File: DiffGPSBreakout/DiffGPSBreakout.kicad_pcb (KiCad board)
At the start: 2 copper layers, 110.2 x 72.3 mm, 16 parts, among them U1 Raspberry_Pi

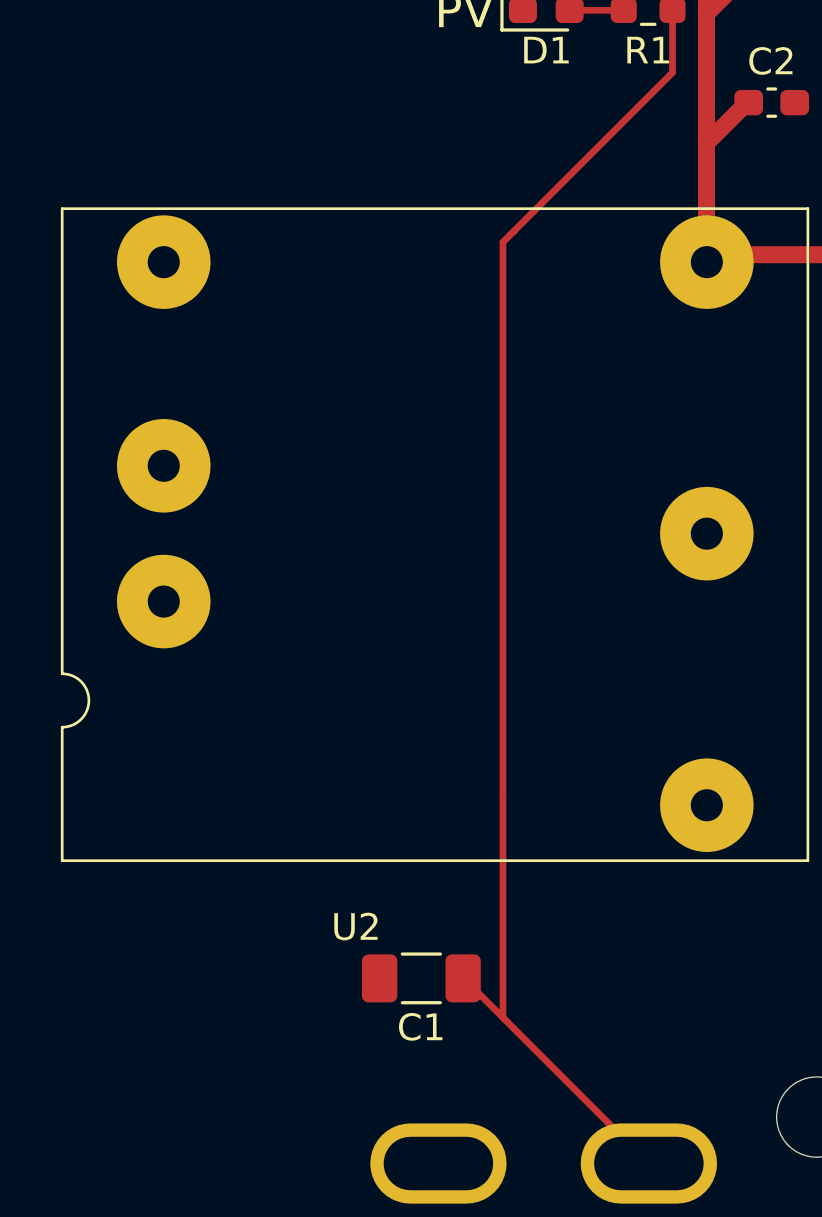
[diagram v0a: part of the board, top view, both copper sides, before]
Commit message: fixed traces
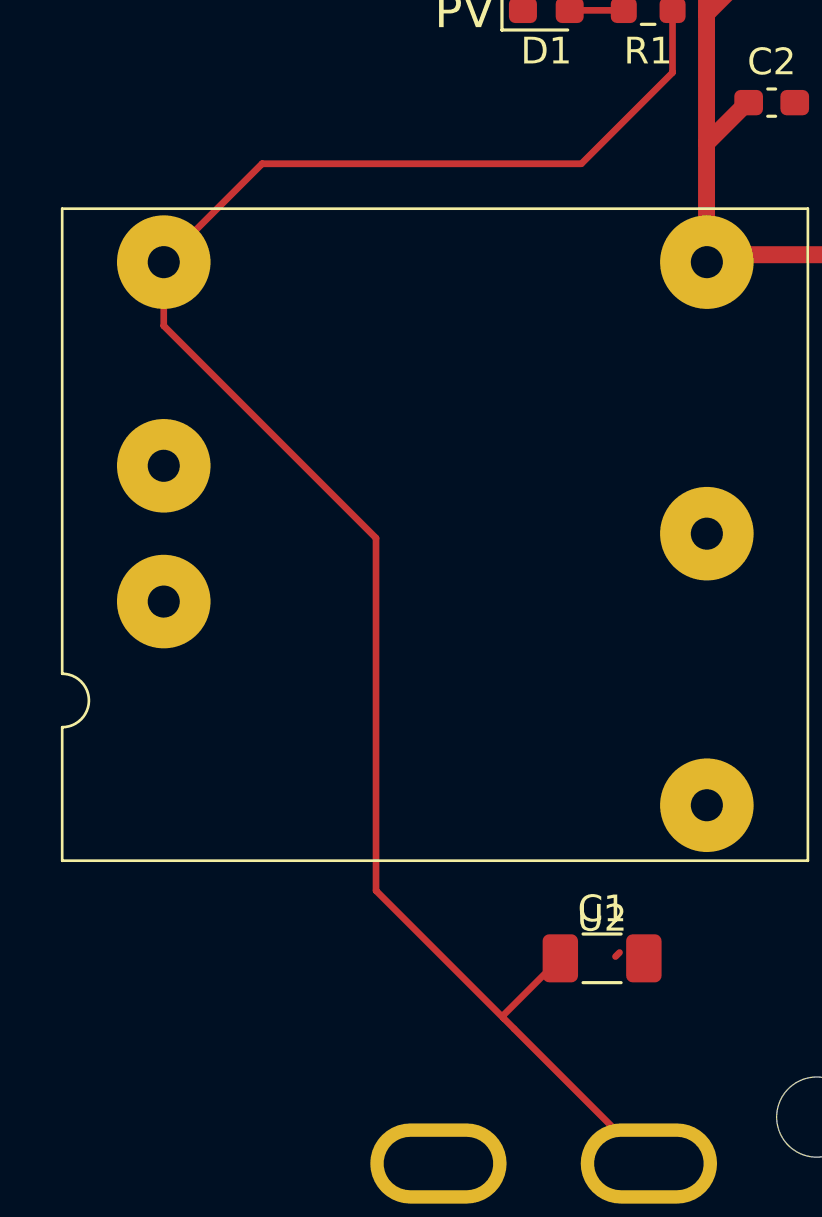
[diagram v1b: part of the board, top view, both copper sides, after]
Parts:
- moved C1 6.80 mm to (106.9, 107.4), turned to 0 degrees
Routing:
- net VCC: track 50.6 -> 69.3 mm
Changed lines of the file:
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@@
 		(at 86.734 103.7432)
 		(property "Reference" "U2"
-			(at 10.999999 2.494519 0)
+			(at 20.2 2.1494 0)
 			(unlocked yes)
 			(layer "F.SilkS")
@@
 		)
 		(property "Value" "~"
-			(at 10.999999 3.994519 0)
+			(at 20.2 3.6494 0)
 			(unlocked yes)
 			(layer "F.Fab")
@@
 		)
 		(fp_text user "${REFERENCE}"
-			(at 10.999999 5.494519 0)
+			(at 20.2 5.1494 0)
 			(unlocked yes)
 			(layer "F.Fab")
@@
 	(footprint "Capacitor_SMD:C_1206_3216Metric_Pad1.33x1.80mm_HandSolder"
 		(layer "F.Cu")
-		(at 100.172119 108.141401 180)
+		(at 106.934 107.3912)
 		(descr "Capacitor SMD 1206 (3216 Metric), square (rectangular) end terminal, IPC_7351 nominal with elongated pad for handsoldering. (Body size source: IPC-SM-782 page 76, https://www.pcb-3d.com/wordpress/wp-content/uploads/ipc-sm-782a_amendment_1_and_2.pdf), generated with kicad-footprint-generator")
 		(tags "capacitor handsolder")
 		(property "Reference" "C1"
-			(at 0 -1.85 180)
+			(at 0 -1.85 360)
 			(layer "F.SilkS")
 			(effects
@@
 		)
 		(property "Value" "10uF"
-			(at 0 1.85 180)
+			(at 0 1.85 360)
 			(layer "F.Fab")
 			(effects
@@
 		)
 		(property "Footprint" ""
-			(at 0 0 180)
+			(at 0 0 360)
 			(layer "F.Fab")
 			(hide yes)
@@
 		)
 		(property "Datasheet" ""
-			(at 0 0 180)
+			(at 0 0 360)
 			(layer "F.Fab")
 			(hide yes)
@@
 		)
 		(property "Description" "Unpolarized capacitor"
-			(at 0 0 180)
+			(at 0 0 360)
 			(layer "F.Fab")
 			(hide yes)
@@
 		(attr smd)
 		(fp_line
-			(start -0.711252 0.91)
-			(end 0.711252 0.91)
+			(start -0.711252 -0.91)
+			(end 0.711252 -0.91)
 			(stroke
 				(width 0.12)
@@
 		)
 		(fp_line
-			(start -0.711252 -0.91)
-			(end 0.711252 -0.91)
+			(start -0.711252 0.91)
+			(end 0.711252 0.91)
 			(stroke
 				(width 0.12)
@@
 		)
 		(fp_line
-			(start 2.48 1.15)
-			(end -2.48 1.15)
+			(start -2.48 -1.15)
+			(end 2.48 -1.15)
 			(stroke
 				(width 0.05)
@@
 		)
 		(fp_line
-			(start 2.48 -1.15)
-			(end 2.48 1.15)
+			(start -2.48 1.15)
+			(end -2.48 -1.15)
 			(stroke
 				(width 0.05)
@@
 		)
 		(fp_line
-			(start -2.48 1.15)
-			(end -2.48 -1.15)
+			(start 2.48 -1.15)
+			(end 2.48 1.15)
 			(stroke
 				(width 0.05)
@@
 		)
 		(fp_line
-			(start -2.48 -1.15)
-			(end 2.48 -1.15)
+			(start 2.48 1.15)
+			(end -2.48 1.15)
 			(stroke
 				(width 0.05)
@@
 		)
 		(fp_line
-			(start 1.6 0.8)
-			(end -1.6 0.8)
+			(start -1.6 -0.8)
+			(end 1.6 -0.8)
 			(stroke
 				(width 0.1)
@@
 		)
 		(fp_line
-			(start 1.6 -0.8)
-			(end 1.6 0.8)
+			(start -1.6 0.8)
+			(end -1.6 -0.8)
 			(stroke
 				(width 0.1)
@@
 		)
 		(fp_line
-			(start -1.6 0.8)
-			(end -1.6 -0.8)
+			(start 1.6 -0.8)
+			(end 1.6 0.8)
 			(stroke
 				(width 0.1)
@@
 		)
 		(fp_line
-			(start -1.6 -0.8)
-			(end 1.6 -0.8)
+			(start 1.6 0.8)
+			(end -1.6 0.8)
 			(stroke
 				(width 0.1)
@@
 		)
 		(fp_text user "${REFERENCE}"
-			(at 0 0 180)
+			(at 0 0 360)
 			(layer "F.Fab")
 			(effects
@@
 		)
 		(pad "1" smd roundrect
-			(at -1.5625 0 180)
+			(at -1.5625 0)
 			(size 1.325 1.8)
 			(layers "F.Cu" "F.Paste" "F.Mask")
@@
 		)
 		(pad "2" smd roundrect
-			(at 1.5625 0 180)
+			(at 1.5625 0)
 			(size 1.325 1.8)
 			(layers "F.Cu" "F.Paste" "F.Mask")
@@
 	)
 	(segment
+		(start 98.4758 104.858882)
+		(end 103.251219 109.634301)
+		(width 0.25)
+		(layer "F.Cu")
+		(net 31)
+	)
+	(segment
 		(start 108.935119 115.318201)
 		(end 103.6396 110.022682)
@@
 	)
 	(segment
-		(start 101.758319 108.141401)
-		(end 103.251219 109.634301)
+		(start 90.534 81.3432)
+		(end 90.534 83.7268)
 		(width 0.25)
 		(layer "F.Cu")
@@
 	)
 	(segment
-		(start 101.734619 108.141401)
-		(end 101.758319 108.141401)
+		(start 98.4758 91.6686)
+		(end 98.4758 104.858882)
 		(width 0.25)
 		(layer "F.Cu")
@@
 	)
 	(segment
-		(start 106.159119 77.662401)
-		(end 103.634119 80.187401)
+		(start 94.214799 77.662401)
+		(end 90.534 81.3432)
 		(width 0.254)
 		(layer "F.Cu")
@@
 	)
 	(segment
-		(start 109.534119 71.958901)
-		(end 109.570119 71.922901)
-		(width 0.254)
-		(layer "F.Cu")
-		(net 31)
-	)
-	(segment
-		(start 103.634119 80.187401)
-		(end 103.6396 80.192882)
-		(width 0.254)
+		(start 105.3715 107.3912)
+		(end 103.251219 109.511481)
+		(width 0.25)
 		(layer "F.Cu")
 		(net 31)
 	)
 	(segment
-		(start 103.2256 109.608682)
+		(start 103.251219 109.511481)
 		(end 103.251219 109.634301)
 		(width 0.25)
@@
 	)
 	(segment
-		(start 103.2256 101.3714)
-		(end 103.2256 109.608682)
-		(width 0.25)
+		(start 109.534119 71.958901)
+		(end 109.570119 71.922901)
+		(width 0.254)
 		(layer "F.Cu")
 		(net 31)
 	)
 	(segment
-		(start 103.634119 80.187401)
-		(end 103.2256 80.59592)
+		(start 107.434901 107.325481)
+		(end 107.587301 107.173081)
 		(width 0.25)
 		(layer "F.Cu")
@@
 	)
 	(segment
-		(start 103.2256 80.59592)
-		(end 103.2256 101.3714)
+		(start 90.534 83.7268)
+		(end 98.4758 91.6686)
 		(width 0.25)
 		(layer "F.Cu")
@@
 		(layer "F.Cu")
 		(net 31)
+	)
+	(segment
+		(start 106.159119 77.662401)
+		(end 94.214799 77.662401)
+		(width 0.254)
+		(layer "F.Cu")
+		(net 31)

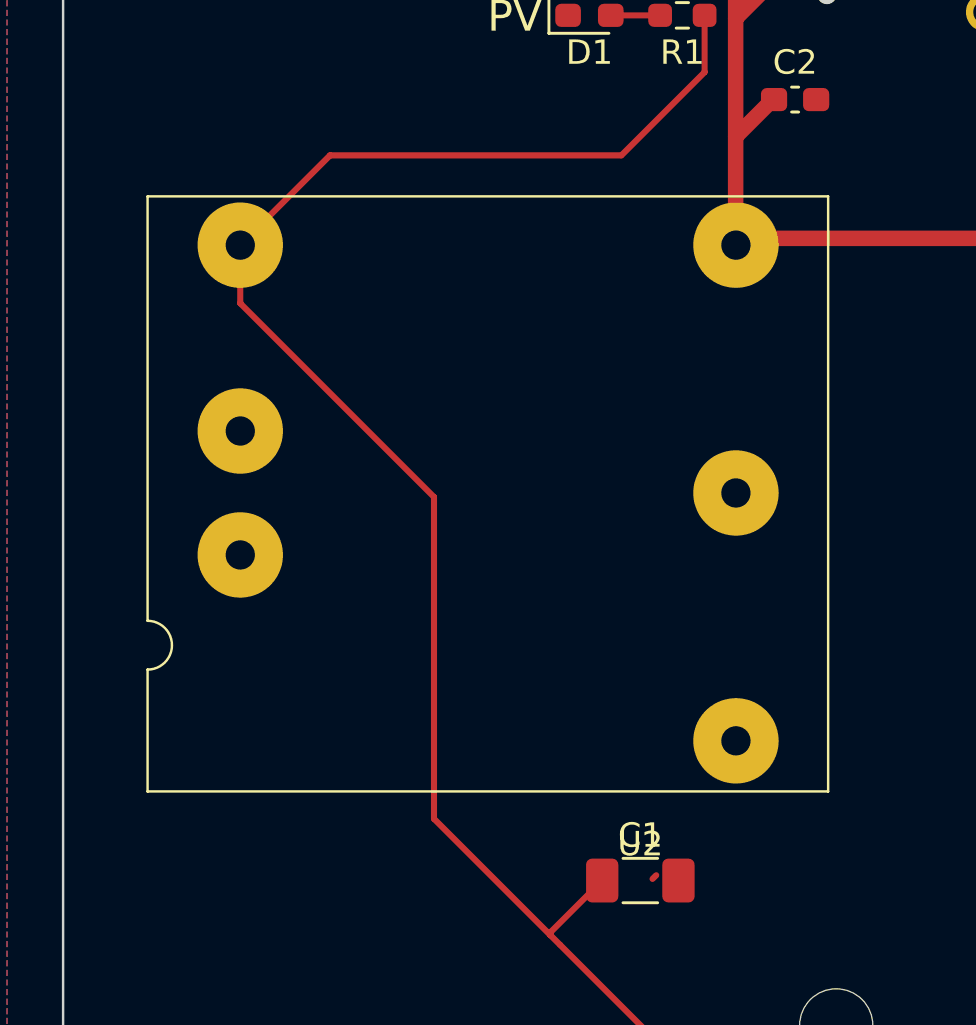
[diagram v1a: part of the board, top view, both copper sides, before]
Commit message: Changed dc-dc converter to be accurate footprint
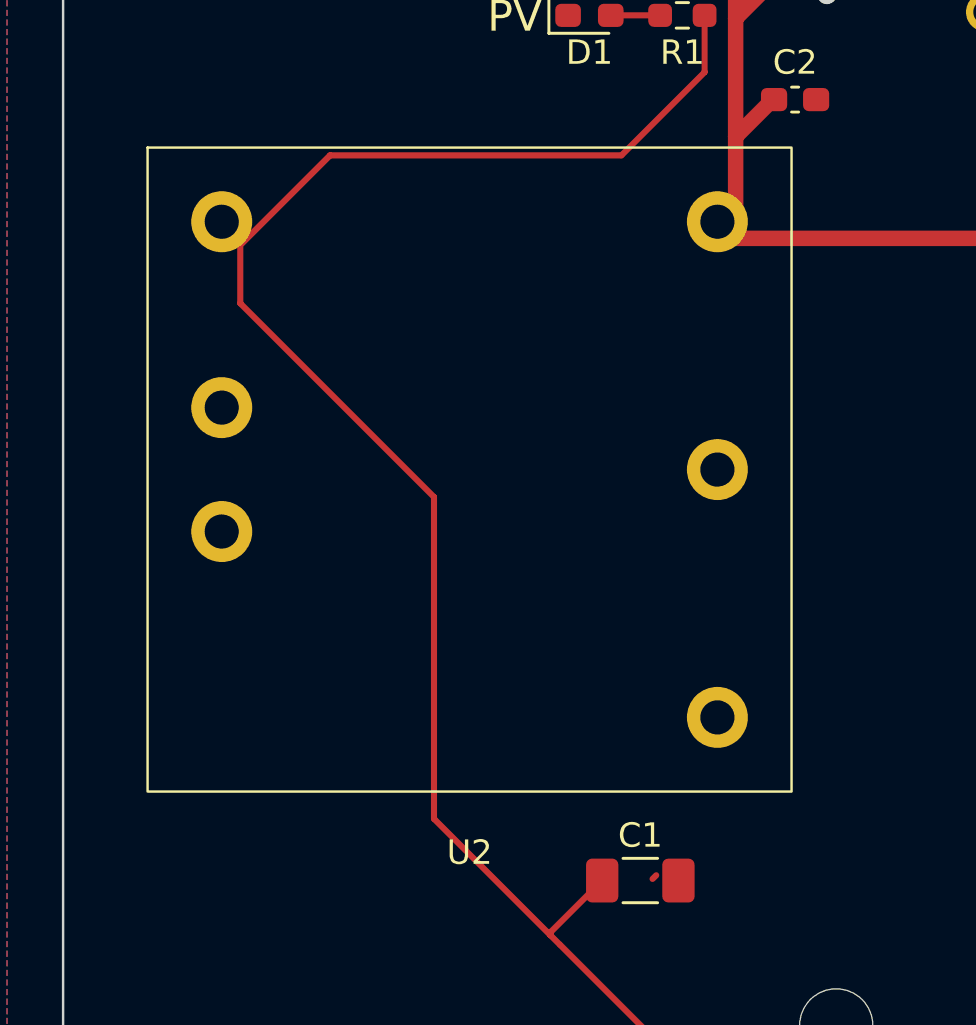
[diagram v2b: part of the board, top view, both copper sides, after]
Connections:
- U2 pad 1: VCC -> GND
- U2 pad 3: GND -> VCC
- U2 pad 4: GND -> +5V
- U2 pad 6: +5V -> GND
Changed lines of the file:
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@@
 		(at 86.734 103.7432)
 		(property "Reference" "U2"
-			(at 20.2 2.1494 0)
+			(at 13.2 2.5 0)
 			(unlocked yes)
 			(layer "F.SilkS")
@@
 		)
 		(property "Value" "~"
-			(at 20.2 3.6494 0)
+			(at 14.76 2.45 0)
 			(unlocked yes)
 			(layer "F.Fab")
@@
 		)
 		(property "Footprint" "MRDT_Devices:PKE3311PI_Through_Hole"
-			(at 0 0 360)
+			(at 13.2 1 0)
 			(layer "F.Fab")
 			(hide yes)
@@
 		)
 		(property "Datasheet" ""
-			(at 0 0 360)
+			(at 0 0 0)
 			(layer "F.Fab")
 			(hide yes)
@@
 		)
 		(property "Description" ""
-			(at 0 0 360)
+			(at 0 0 0)
 			(layer "F.Fab")
 			(hide yes)
@@
 		)
 		(attr smd)
-		(fp_line
-			(start -0.000001 -0.005481)
-			(end 27.899999 -0.005481)
+		(fp_rect
+			(start 0 -26.4)
+			(end 26.4 0)
 			(stroke
 				(width 0.1)
 				(type default)
 			)
-			(layer "F.SilkS")
-		)
-		(fp_line
-			(start 0 -7)
-			(end 0 -24.4)
-			(stroke
-				(width 0.1)
-				(type default)
-			)
-			(layer "F.SilkS")
-		)
-		(fp_line
-			(start 0 -5)
-			(end 0 0)
-			(stroke
-				(width 0.1)
-				(type default)
-			)
-			(layer "F.SilkS")
-		)
-		(fp_line
-			(start 27.9 -24.4)
-			(end 0 -24.4)
-			(stroke
-				(width 0.1)
-				(type default)
-			)
-			(layer "F.SilkS")
-		)
-		(fp_line
-			(start 27.9 0)
-			(end 27.9 -24.4)
-			(stroke
-				(width 0.1)
-				(type default)
-			)
-			(layer "F.SilkS")
-		)
-		(fp_arc
-			(start 0 -7)
-			(mid 1 -6)
-			(end 0 -5)
-			(stroke
-				(width 0.1)
-				(type default)
-			)
+			(fill none)
 			(layer "F.SilkS")
 		)
 		(fp_text user "${REFERENCE}"
-			(at 20.2 5.1494 0)
+			(at 13.2 4.35 0)
 			(unlocked yes)
 			(layer "F.Fab")
@@
 		)
 		(pad "1" thru_hole circle
-			(at 3.8 -22.4)
-			(size 3.5 3.5)
-			(drill 1.2)
+			(at 3.04 -23.36)
+			(size 2.5 2.5)
+			(drill 1.4)
 			(layers "*.Cu" "*.Mask")
 			(remove_unused_layers no)
-			(net 31 "VCC")
+			(net 10 "GND")
 			(pinfunction "Vin+")
 			(pintype "input")
 		)
 		(pad "2" thru_hole circle
-			(at 3.8 -14.78)
-			(size 3.5 3.5)
-			(drill 1.2)
+			(at 3.04 -15.74)
+			(size 2.5 2.5)
+			(drill 1.4)
 			(layers "*.Cu" "*.Mask")
 			(remove_unused_layers no)
@@
 		)
 		(pad "3" thru_hole circle
-			(at 3.8 -9.7)
-			(size 3.5 3.5)
-			(drill 1.2)
+			(at 3.04 -10.66)
+			(size 2.5 2.5)
+			(drill 1.4)
 			(layers "*.Cu" "*.Mask")
 			(remove_unused_layers no)
-			(net 10 "GND")
+			(net 31 "VCC")
 			(pinfunction "On/OFF")
 			(pintype "input")
 		)
 		(pad "4" thru_hole circle
-			(at 24.12 -2.08)
-			(size 3.5 3.5)
-			(drill 1.2)
+			(at 23.36 -3.04)
+			(size 2.5 2.5)
+			(drill 1.4)
 			(layers "*.Cu" "*.Mask")
 			(remove_unused_layers no)
-			(net 10 "GND")
+			(net 25 "+5V")
 			(pinfunction "Vout-")
 			(pintype "output")
 		)
 		(pad "5" thru_hole circle
-			(at 24.12 -12.24)
-			(size 3.5 3.5)
-			(drill 1.2)
+			(at 23.36 -13.2)
+			(size 2.5 2.5)
+			(drill 1.4)
 			(layers "*.Cu" "*.Mask")
 			(remove_unused_layers no)
@@
 		)
 		(pad "6" thru_hole circle
-			(at 24.12 -22.4)
-			(size 3.5 3.5)
-			(drill 1.2)
+			(at 23.36 -23.36)
+			(size 2.5 2.5)
+			(drill 1.4)
 			(layers "*.Cu" "*.Mask")
 			(remove_unused_layers no)
-			(net 25 "+5V")
+			(net 10 "GND")
 			(pinfunction "Vout+")
 			(pintype "output")
@@
 		(tags "capacitor handsolder")
 		(property "Reference" "C1"
-			(at 0 -1.85 360)
+			(at 0 -1.85 0)
 			(layer "F.SilkS")
 			(effects
@@
 		)
 		(property "Value" "10uF"
-			(at 0 1.85 360)
+			(at 0 1.85 0)
 			(layer "F.Fab")
 			(effects
@@
 		)
 		(property "Footprint" ""
-			(at 0 0 360)
+			(at 0 0 0)
 			(layer "F.Fab")
 			(hide yes)
@@
 		)
 		(property "Datasheet" ""
-			(at 0 0 360)
+			(at 0 0 0)
 			(layer "F.Fab")
 			(hide yes)
@@
 		)
 		(property "Description" "Unpolarized capacitor"
-			(at 0 0 360)
+			(at 0 0 0)
 			(layer "F.Fab")
 			(hide yes)
@@
 		)
 		(fp_text user "${REFERENCE}"
-			(at 0 0 360)
-			(layer "F.Fab")
-			(effects
+			(at 0 0 0)
+			(layer "F.Fab")
+			(effects
